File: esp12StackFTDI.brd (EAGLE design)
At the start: 31.5 x 30 mm, 31 parts, among them J02 470, J04 470, J05 470, J12 470, J13 470

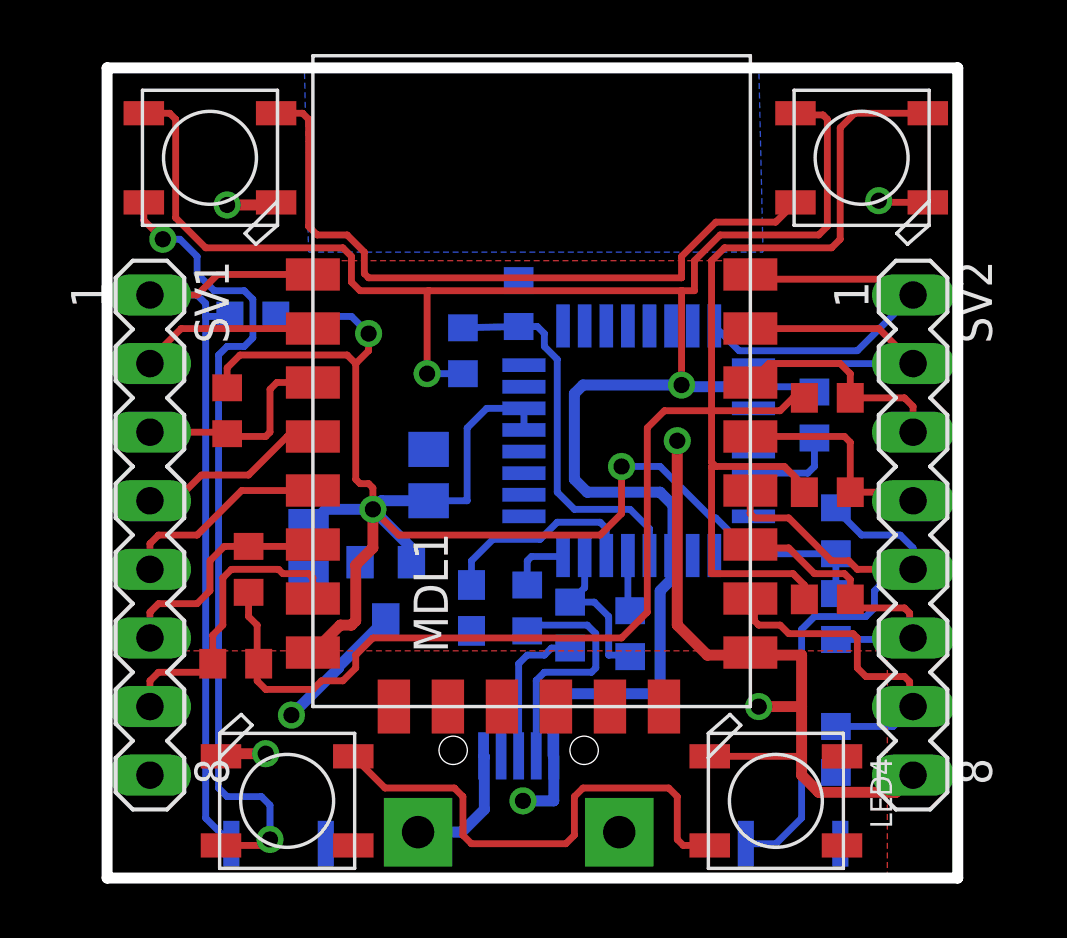
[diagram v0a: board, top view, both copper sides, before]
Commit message: minor routing changes
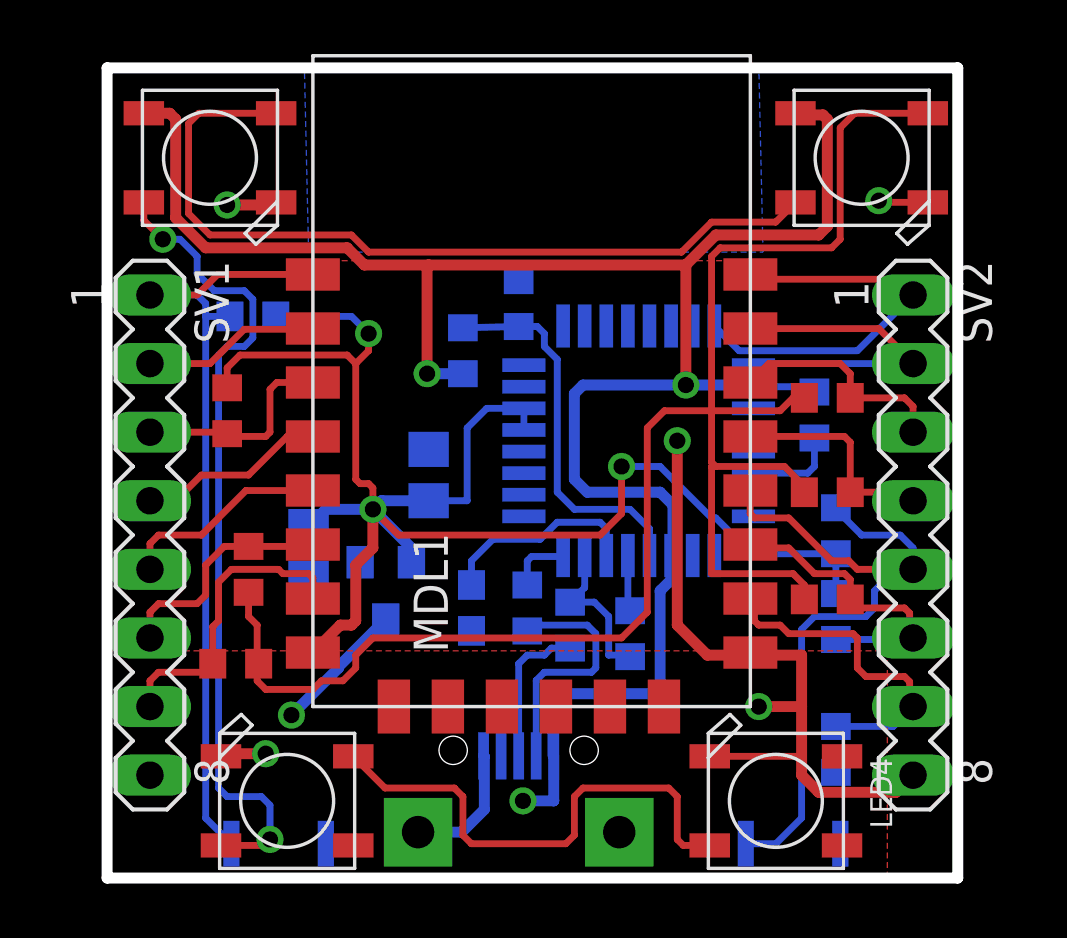
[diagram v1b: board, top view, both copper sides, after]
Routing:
- net DOUT1DIN2: track 26.3 -> 30.7 mm

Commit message: Deep Sleep capability
added a jumper Position to connect GIPO16 and REST to enable wake up from deep sleep.
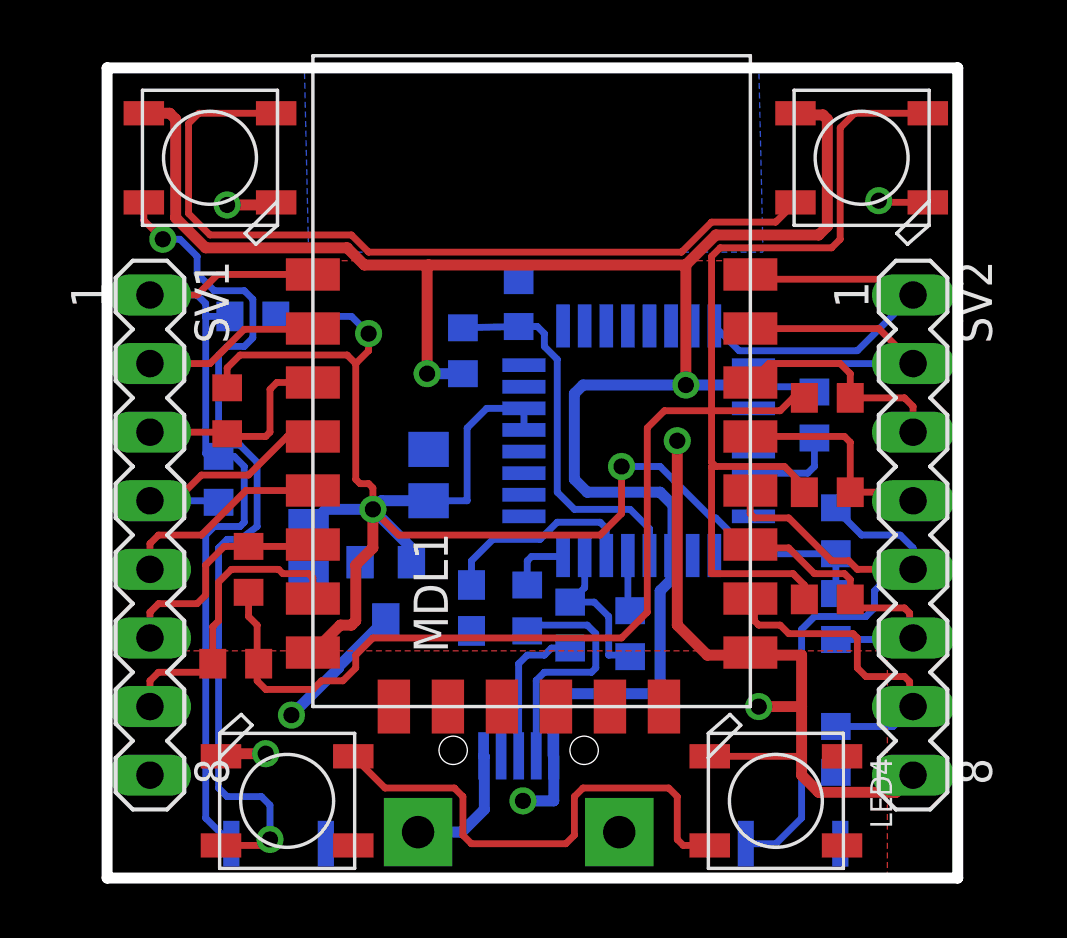
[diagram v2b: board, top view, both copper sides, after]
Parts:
- added J_REST: 10k, eagle-ltspice:R0603
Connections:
- net GPIO16: now also J_REST.1
- net REST: now also J_REST.2
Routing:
- net GPIO16: track 7.27 -> 10.3 mm
- net REST: track 29.8 -> 32.7 mm
- net DOUT2DIN3: track 30.6 -> 32.5 mm
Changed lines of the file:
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@@
 <attribute name="SPICEPREFIX" value="R" x="15.24" y="21.2725" size="1.778" layer="28" rot="MR90" display="off"/>
+</element>
+<element name="J_REST" library="eagle-ltspice" package="R0603" value="10k" x="4.1275" y="14.76375" rot="MR90">
+<attribute name="SPICEPREFIX" value="R" x="4.1275" y="14.76375" size="1.778" layer="28" rot="MR90" display="off"/>
+<attribute name="SPICEMODEL" value="NONE" x="4.1275" y="14.76375" size="1.778" layer="28" rot="MR90" display="off"/>
 </element>
 </elements>
@@
 <wire x1="3.33375" y1="21.59" x2="3.65125" y2="21.2725" width="0.254" layer="16"/>
 <wire x1="3.65125" y1="21.2725" x2="3.65125" y2="20.79625" width="0.254" layer="16"/>
-<wire x1="3.65125" y1="20.79625" x2="3.65125" y2="2.21875" width="0.254" layer="16"/>
 <wire x1="3.65125" y1="2.21875" x2="4.6" y2="1.27" width="0.254" layer="16"/>
 <wire x1="7.62" y1="22.35" x2="4.09375" y2="22.35" width="0.254" layer="1"/>
 <wire x1="4.09375" y1="22.35" x2="3.33375" y2="21.59" width="0.254" layer="1"/>
 <wire x1="3.33375" y1="21.59" x2="1.5875" y2="21.59" width="0.254" layer="1"/>
+<contactref element="J_REST" pad="2"/>
 <wire x1="4.5475" y1="20.79625" x2="3.65125" y2="20.79625" width="0.254" layer="16"/>
+<wire x1="3.65125" y1="20.79625" x2="3.65125" y2="15.71625" width="0.254" layer="16"/>
+<wire x1="3.65125" y1="15.71625" x2="3.81" y2="15.5575" width="0.254" layer="16"/>
+<wire x1="3.81" y1="15.5575" x2="4.38875" y2="15.5575" width="0.254" layer="16"/>
+<wire x1="4.38875" y1="15.5575" x2="4.1275" y2="15.61375" width="0.254" layer="16"/>
+<wire x1="4.1275" y1="15.61375" x2="4.70625" y2="15.61375" width="0.254" layer="16"/>
+<wire x1="4.92125" y1="13.0175" x2="3.96875" y2="13.0175" width="0.254" layer="16"/>
+<wire x1="3.65125" y1="12.7" x2="3.65125" y2="2.21875" width="0.254" layer="16"/>
+<wire x1="3.96875" y1="13.0175" x2="3.65125" y2="12.7" width="0.254" layer="16"/>
+<wire x1="4.70625" y1="15.61375" x2="5.08" y2="15.24" width="0.254" layer="16"/>
+<wire x1="5.08" y1="15.24" x2="5.08" y2="13.17625" width="0.254" layer="16"/>
+<wire x1="5.08" y1="13.17625" x2="4.92125" y2="13.0175" width="0.254" layer="16"/>
 </signal>
 <signal name="ADC">
@@
 <wire x1="3.4925" y1="14.9225" x2="5.23875" y2="14.9225" width="0.254" layer="1"/>
 <wire x1="5.23875" y1="14.9225" x2="6.66625" y2="16.35" width="0.254" layer="1"/>
+<contactref element="J_REST" pad="1"/>
+<wire x1="1.5875" y1="13.97" x2="4.38875" y2="13.97" width="0.254" layer="16"/>
+<wire x1="4.38875" y1="13.97" x2="4.1275" y2="13.91375" width="0.254" layer="16"/>
 </signal>
 <signal name="GPIO14">
@@
 <wire x1="2.69875" y1="23.65375" x2="3.33375" y2="23.01875" width="0.254" layer="16"/>
 <via x="6.0325" y="1.42875" extent="1-16" drill="0.6"/>
-<wire x1="5.3975" y1="20.0025" x2="5.08" y2="19.685" width="0.254" layer="16"/>
-<wire x1="5.08" y1="19.685" x2="4.445" y2="19.685" width="0.254" layer="16"/>
-<wire x1="4.445" y1="19.685" x2="4.1275" y2="19.3675" width="0.254" layer="16"/>
-<wire x1="4.1275" y1="19.3675" x2="4.1275" y2="3.33375" width="0.254" layer="16"/>
-<wire x1="4.1275" y1="3.33375" x2="4.445" y2="3.01625" width="0.254" layer="16"/>
 <wire x1="4.445" y1="3.01625" x2="5.715" y2="3.01625" width="0.254" layer="16"/>
 <wire x1="5.715" y1="3.01625" x2="6.0325" y2="2.69875" width="0.254" layer="16"/>
@@
 <wire x1="3.96875" y1="21.74875" x2="5.08" y2="21.74875" width="0.254" layer="16"/>
 <wire x1="5.08" y1="21.74875" x2="5.3975" y2="21.43125" width="0.254" layer="16"/>
-<wire x1="5.3975" y1="21.43125" x2="5.3975" y2="20.0025" width="0.254" layer="16"/>
 <wire x1="4.2175" y1="1.2075" x2="5.81125" y2="1.2075" width="0.254" layer="1"/>
 <wire x1="5.81125" y1="1.2075" x2="6.0325" y2="1.42875" width="0.254" layer="1"/>
+<wire x1="5.3975" y1="21.43125" x2="5.3975" y2="20.0025" width="0.254" layer="16"/>
+<wire x1="5.3975" y1="20.0025" x2="5.08" y2="19.685" width="0.254" layer="16"/>
+<wire x1="5.08" y1="19.685" x2="4.445" y2="19.685" width="0.254" layer="16"/>
+<wire x1="4.445" y1="19.685" x2="4.1275" y2="19.3675" width="0.254" layer="16"/>
+<wire x1="4.1275" y1="19.3675" x2="4.1275" y2="16.1925" width="0.254" layer="16"/>
+<wire x1="4.1275" y1="16.1925" x2="4.28625" y2="16.03375" width="0.254" layer="16"/>
+<wire x1="4.28625" y1="16.03375" x2="4.92125" y2="16.03375" width="0.254" layer="16"/>
+<wire x1="4.92125" y1="12.54125" x2="4.445" y2="12.54125" width="0.254" layer="16"/>
+<wire x1="4.445" y1="12.54125" x2="4.1275" y2="12.22375" width="0.254" layer="16"/>
+<wire x1="4.1275" y1="12.22375" x2="4.1275" y2="3.33375" width="0.254" layer="16"/>
+<wire x1="4.1275" y1="3.33375" x2="4.445" y2="3.01625" width="0.254" layer="16"/>
+<wire x1="4.92125" y1="16.03375" x2="5.55625" y2="15.39875" width="0.254" layer="16"/>
+<wire x1="5.55625" y1="15.39875" x2="5.55625" y2="13.0175" width="0.254" layer="16"/>
+<wire x1="5.55625" y1="13.0175" x2="4.92125" y2="12.54125" width="0.254" layer="16"/>
 </signal>
 <signal name="DOUT3DIN4">
